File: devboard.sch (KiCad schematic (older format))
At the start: 93 parts, among them J1 Conn_01x04, J2 Conn_02x05_Odd_Even, J3 USB_B_Micro, J4 Conn_01x04, J5 Conn_02x10_Counter_Clockwise, J6 Conn_02x04_Counter_Clockwise, Q1 Q_NPN_BEC, Q2 Q_NPN_BEC, SW1 SW_SPST, U1 ATmega128L-8AU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

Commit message: Remove extraneous wire
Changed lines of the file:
@@
 	1200 1800 1200 1850
 Wire Wire Line
-	1500 1850 1200 1850
-Wire Wire Line
 	1500 2150 1500 2200
 Connection ~ 1500 2200
@@
 Text Label 1900 4900 0    50   ~ 0
 ~OE
-$Comp
-L MCU_Microchip_ATmega:ATmega128L-8AU U1
-U 1 1 5FDDF59E
-P 2650 3900
-F 0 "U1" H 1850 6050 50  0000 C CNN
-F 1 "ATmega128L-8AU" H 2150 5950 50  0000 C CNN
-F 2 "Package_QFP:TQFP-64_14x14mm_P0.8mm" H 2650 3900 50  0001 C CIN
-F 3 "http://ww1.microchip.com/downloads/en/DeviceDoc/doc2467.pdf" H 2650 3900 50  0001 C CNN
-	1    2650 3900
-	1    0    0    -1
-$EndComp
 Wire Wire Line
 	1900 4900 2050 4900
@@
 Wire Wire Line
 	14750 9350 14750 9400
-Connection ~ 14650 1400
-Wire Wire Line
-	14650 1400 15000 1400
 Wire Wire Line
 	8200 4700 8200 4850
@@
 	13600 8600 13600 8650
 Wire Bus Line
-	11700 10350 11700 10750
-Wire Bus Line
-	10700 10350 10700 10750
+	8200 5450 8200 7500
 Wire Bus Line
 	9500 5850 9500 7650
 Wire Bus Line
+	10800 5450 10800 7500
+Wire Bus Line
 	12100 5850 12100 7650
 Wire Bus Line
+	13400 5450 13400 7500
+Wire Bus Line
 	14700 5850 14700 7650
 Wire Bus Line
+	10250 9750 10250 10750
+Wire Bus Line
 	9250 9750 9250 10750
 Wire Bus Line
-	9500 2400 9500 4200
+	11700 10350 11700 10750
 Wire Bus Line
-	12100 2400 12100 4200
+	10700 10350 10700 10750
 Wire Bus Line
-	14700 2400 14700 4200
+	8200 2000 8200 4050
 Wire Bus Line
-	3500 2050 3500 2800
+	9500 2400 9500 4200
 Wire Bus Line
-	10250 9750 10250 10750
+	10800 2000 10800 4050
 Wire Bus Line
-	3500 2950 3500 5500
+	12100 2400 12100 4200
 Wire Bus Line
 	13400 2000 13400 4050
 Wire Bus Line
-	10800 2000 10800 4050
-Wire Bus Line
-	8200 2000 8200 4050
-Wire Bus Line
-	13400 5450 13400 7500
+	14700 2400 14700 4200
 Wire Bus Line
-	10800 5450 10800 7500
+	3500 2950 3500 5500
 Wire Bus Line
-	8200 5450 8200 7500
+	3500 2050 3500 2800
+Wire Wire Line
+	1500 1850 1200 1850
+$Comp
+L MCU_Microchip_ATmega:ATmega128L-8AU U1
+U 1 1 5FDDF59E
+P 2650 3900
+F 0 "U1" H 1850 6050 50  0000 C CNN
+F 1 "ATmega128L-8AU" H 2150 5950 50  0000 C CNN
+F 2 "Package_QFP:TQFP-64_14x14mm_P0.8mm" H 2650 3900 50  0001 C CIN
+F 3 "http://ww1.microchip.com/downloads/en/DeviceDoc/doc2467.pdf" H 2650 3900 50  0001 C CNN
+	1    2650 3900
+	1    0    0    -1
+$EndComp
 $EndSCHEMATC

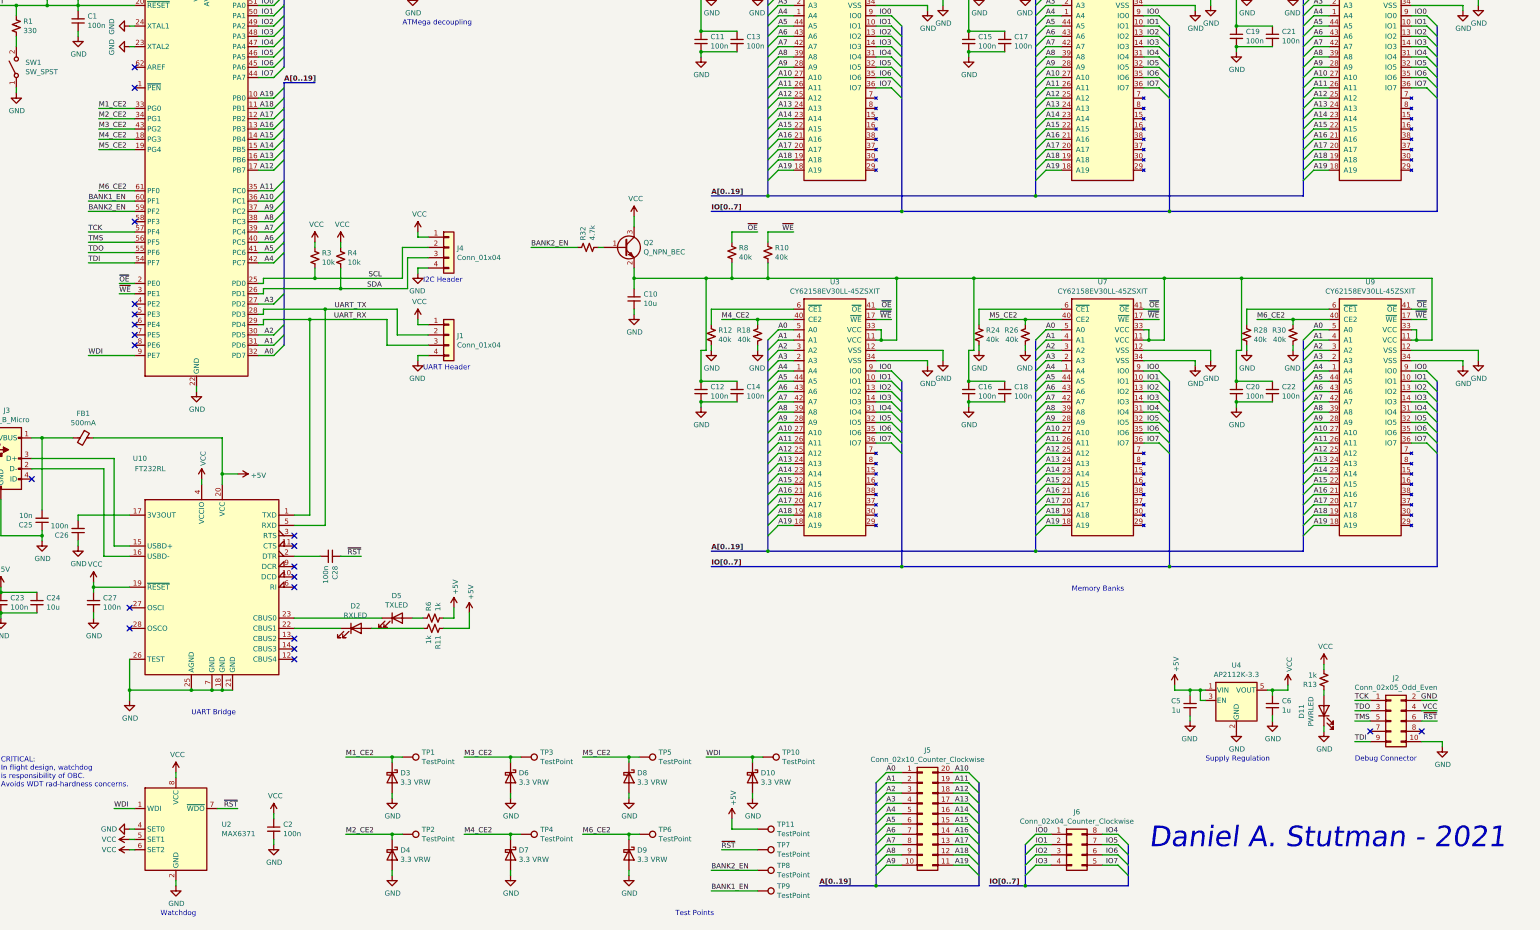
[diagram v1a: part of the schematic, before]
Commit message: SPI programming and silk improvements
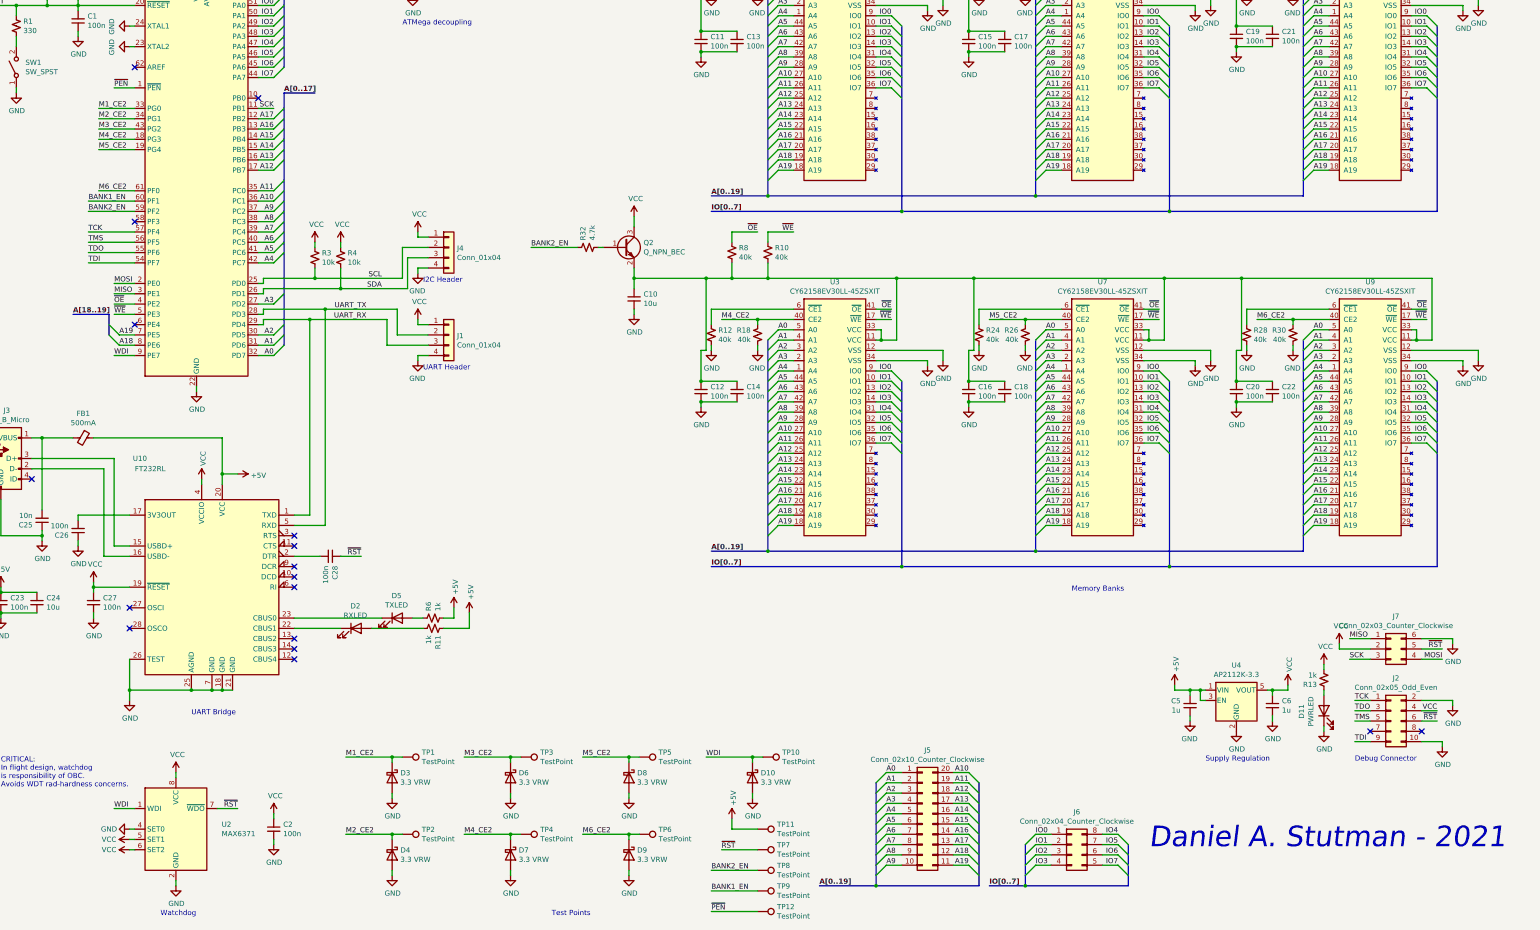
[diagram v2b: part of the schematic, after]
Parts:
- added J7: Conn_02x03_Counter_Clockwise, Connector_PinHeader_1.27mm:PinHeader_2x03_P1.27mm_Vertical, symbol Connector_Generic:Conn_02x03_Counter_Clockwise
- added TP12: TestPoint, Connector_PinHeader_2.54mm:PinHeader_1x01_P2.54mm_Vertical, symbol Connector:TestPoint
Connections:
- net A18: now also U1.8 (PE6); no longer U1.11 (PB1)
- net A19: now also U1.7 (PE5); no longer U1.10 (PB0)
- net GND: now also J7.6 (Pin_6)
- net VCC: now also J7.2 (Pin_2)
- net ~OE: now also U1.4 (PE2); no longer U1.2 (PE0)
- net ~RST: now also J7.5 (Pin_5)
- net ~WE: now also U1.5 (PE3); no longer U1.3 (PE1)
- net ~PEN: now reaches U1.1 (~PEN)
- net ~PEN: now also TP12.1
- new net MISO: J7.1 (Pin_1), U1.3 (PE1)
- new net MOSI: J7.4 (Pin_4), U1.2 (PE0)
- new net SCK: J7.3 (Pin_3), U1.11 (PB1)
- no-connect marks 21 -> 17
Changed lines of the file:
@@
 	1    0    0    -1
 $EndComp
-Text Label 1600 5600 0    50   ~ 0
+Text Label 1850 5600 0    50   ~ 0
 WDI
 Wire Wire Line
-	1600 5600 2050 5600
-Wire Wire Line
 	1600 4400 2050 4400
 Wire Wire Line
@@
 A17
 Entry Wire Line
-	3500 3100 3400 3200
-Text Label 3400 3200 2    50   ~ 0
+	1800 5400 1900 5500
+Text Label 1900 5500 0    50   ~ 0
 A18
 Entry Wire Line
-	3500 3000 3400 3100
-Text Label 3400 3100 2    50   ~ 0
+	1800 5300 1900 5400
+Text Label 1900 5400 0    50   ~ 0
 A19
 Wire Wire Line
@@
 	3400 3300 3250 3300
 Wire Wire Line
-	3400 3200 3250 3200
+	1900 5500 2050 5500
 Wire Wire Line
-	3400 3100 3250 3100
+	1900 5400 2050 5400
 Wire Wire Line
 	3400 3600 3250 3600
@@
 Text Label 3400 4200 2    50   ~ 0
 A9
-Wire Bus Line
-	3500 2950 3800 2950
 Wire Wire Line
 	3300 4850 3300 4900
@@
 Wire Wire Line
 	3300 5300 3250 5300
-Text Label 3500 2950 0    50   ~ 10
-A[0..19]
 Wire Wire Line
 	1700 3200 2050 3200
@@
 TDI
 Wire Wire Line
-	14700 8950 14550 8950
-Wire Wire Line
 	14700 9050 14550 9050
 Wire Wire Line
 	14700 9150 14550 9150
-Text Label 14700 8950 2    50   ~ 0
-GND
 Text Label 14700 9050 2    50   ~ 0
 VCC
@@
 ~RST
 NoConn ~ 14550 9250
-$Comp
-L Connector_Generic:Conn_02x05_Odd_Even J2
-U 1 1 5FDF7679
-P 14250 9150
-F 0 "J2" H 14300 9567 50  0000 C CNN
-F 1 "Conn_02x05_Odd_Even" H 14300 9476 50  0000 C CNN
-F 2 "Connector_PinHeader_1.27mm:PinHeader_2x05_P1.27mm_Vertical" H 14250 9150 50  0001 C CNN
-F 3 "~" H 14250 9150 50  0001 C CNN
-	1    14250 9150
-	1    0    0    -1
-$EndComp
 NoConn ~ 14050 9250
 Text Notes 13900 9550 0    50   ~ 0
@@
 	1    0    0    -1
 $EndComp
-Text Notes 7300 11050 0    50   ~ 0
+Text Notes 6100 11050 0    50   ~ 0
 Test Points
 $Comp
@@
 	3750 5250 4500 5250
 Connection ~ 3750 5250
-NoConn ~ 2050 5100
-NoConn ~ 2050 5200
 NoConn ~ 2050 5300
-NoConn ~ 2050 5400
-NoConn ~ 2050 5500
-NoConn ~ 2050 3000
 NoConn ~ 2050 4300
 Wire Wire Line
@@
 Wire Wire Line
 	8200 4400 8450 4400
-Text Label 1900 5000 0    50   ~ 0
+Text Label 1850 5200 0    50   ~ 0
 ~WE
-Text Label 1900 4900 0    50   ~ 0
+Text Label 1850 5100 0    50   ~ 0
 ~OE
-Wire Wire Line
-	1900 4900 2050 4900
-Wire Wire Line
-	2050 5000 1900 5000
 $Comp
 L power:GND #PWR0121
@@
 Wire Wire Line
 	13600 8600 13600 8650
+Wire Wire Line
+	1500 1850 1200 1850
+$Comp
+L power:GND #PWR0126
+U 1 1 61890DA6
+P 14850 9000
+F 0 "#PWR0126" H 14850 8750 50  0001 C CNN
+F 1 "GND" H 14855 8827 50  0000 C CNN
+F 2 "" H 14850 9000 50  0001 C CNN
+F 3 "" H 14850 9000 50  0001 C CNN
+	1    14850 9000
+	1    0    0    -1
+$EndComp
+$Comp
+L Connector_Generic:Conn_02x05_Odd_Even J2
+U 1 1 5FDF7679
+P 14250 9150
+F 0 "J2" H 14300 9567 50  0000 C CNN
+F 1 "Conn_02x05_Odd_Even" H 14300 9476 50  0000 C CNN
+F 2 "Connector_PinHeader_1.27mm:PinHeader_2x05_P1.27mm_Vertical" H 14250 9150 50  0001 C CNN
+F 3 "~" H 14250 9150 50  0001 C CNN
+	1    14250 9150
+	1    0    0    -1
+$EndComp
+Wire Wire Line
+	14550 8950 14850 8950
+Wire Wire Line
+	14850 8950 14850 9000
+$Comp
+L Connector_Generic:Conn_02x03_Counter_Clockwise J7
+U 1 1 619E5A6C
+P 14250 8450
+F 0 "J7" H 14300 8767 50  0000 C CNN
+F 1 "Conn_02x03_Counter_Clockwise" H 14300 8676 50  0000 C CNN
+F 2 "Connector_PinHeader_1.27mm:PinHeader_2x03_P1.27mm_Vertical" H 14250 8450 50  0001 C CNN
+F 3 "~" H 14250 8450 50  0001 C CNN
+	1    14250 8450
+	1    0    0    -1
+$EndComp
+$Comp
+L power:VCC #PWR0128
+U 1 1 619E68EF
+P 13750 8400
+F 0 "#PWR0128" H 13750 8250 50  0001 C CNN
+F 1 "VCC" H 13765 8573 50  0000 C CNN
+F 2 "" H 13750 8400 50  0001 C CNN
+F 3 "" H 13750 8400 50  0001 C CNN
+	1    13750 8400
+	1    0    0    -1
+$EndComp
+Text Label 1850 4900 0    50   ~ 0
+MOSI
+Text Label 1850 5000 0    50   ~ 0
+MISO
+Text Label 3400 3200 2    50   ~ 0
+SCK
+Wire Wire Line
+	1850 4900 2050 4900
+Wire Wire Line
+	2050 5000 1850 5000
+Wire Wire Line
+	3400 3200 3250 3200
+Text Label 3500 3050 0    50   ~ 10
+A[0..17]
 Wire Bus Line
-	8200 5450 8200 7500
+	3500 3050 3800 3050
+Text Label 1450 5200 0    50   ~ 10
+A[18..19]
 Wire Bus Line
-	9500 5850 9500 7650
+	1450 5200 1800 5200
+$Comp
+L MCU_Microchip_ATmega:ATmega128L-8AU U1
+U 1 1 5FDDF59E
+P 2650 3900
+F 0 "U1" H 1850 6050 50  0000 C CNN
+F 1 "ATmega128L-8AU" H 2150 5950 50  0000 C CNN
+F 2 "Package_QFP:TQFP-64_14x14mm_P0.8mm" H 2650 3900 50  0001 C CIN
+F 3 "http://ww1.microchip.com/downloads/en/DeviceDoc/doc2467.pdf" H 2650 3900 50  0001 C CNN
+	1    2650 3900
+	1    0    0    -1
+$EndComp
+Text Label 1850 3000 0    50   ~ 0
+~PEN
+Wire Wire Line
+	1850 3000 2050 3000
+Text Label 7650 11000 0    50   ~ 0
+~PEN
+$Comp
+L Connector:TestPoint TP12
+U 1 1 62B0EF34
+P 8100 11000
+F 0 "TP12" V 8054 11188 50  0000 L CNN
+F 1 "TestPoint" V 8145 11188 50  0000 L CNN
+F 2 "Connector_PinHeader_2.54mm:PinHeader_1x01_P2.54mm_Vertical" H 8300 11000 50  0001 C CNN
+F 3 "~" H 8300 11000 50  0001 C CNN
+	1    8100 11000
+	0    1    1    0
+$EndComp
+Wire Wire Line
+	7650 11000 8100 11000
+Wire Wire Line
+	1850 5100 2050 5100
+Wire Wire Line
+	1850 5200 2050 5200
+Text Label 14750 8550 2    50   ~ 0
+MOSI
+Text Label 13850 8350 0    50   ~ 0
+MISO
+Wire Wire Line
+	14750 8550 14550 8550
+Wire Wire Line
+	14050 8350 13850 8350
+Text Label 13850 8550 0    50   ~ 0
+SCK
+NoConn ~ 3250 3100
+Wire Wire Line
+	13750 8450 13750 8400
+Wire Wire Line
+	13750 8450 14050 8450
+$Comp
+L power:GND #PWR0130
+U 1 1 61B3CB80
+P 14850 8400
+F 0 "#PWR0130" H 14850 8150 50  0001 C CNN
+F 1 "GND" H 14855 8227 50  0000 C CNN
+F 2 "" H 14850 8400 50  0001 C CNN
+F 3 "" H 14850 8400 50  0001 C CNN
+	1    14850 8400
+	1    0    0    -1
+$EndComp
+Wire Wire Line
+	14850 8400 14850 8350
+Wire Wire Line
+	14850 8350 14550 8350
+Text Label 14750 8450 2    50   ~ 0
+~RST
+Wire Wire Line
+	14550 8450 14750 8450
+Wire Wire Line
+	1850 5600 2050 5600
+Wire Wire Line
+	13850 8550 14050 8550
 Wire Bus Line
-	10800 5450 10800 7500
+	1800 5200 1800 5400
 Wire Bus Line
-	12100 5850 12100 7650
+	11700 10350 11700 10750
 Wire Bus Line
-	13400 5450 13400 7500
+	10700 10350 10700 10750
 Wire Bus Line
-	14700 5850 14700 7650
+	9500 5850 9500 7650
 Wire Bus Line
-	10250 9750 10250 10750
+	12100 5850 12100 7650
+Wire Bus Line
+	14700 5850 14700 7650
 Wire Bus Line
 	9250 9750 9250 10750
 Wire Bus Line
-	11700 10350 11700 10750
+	9500 2400 9500 4200
 Wire Bus Line
-	10700 10350 10700 10750
+	12100 2400 12100 4200
 Wire Bus Line
-	8200 2000 8200 4050
+	14700 2400 14700 4200
 Wire Bus Line
-	9500 2400 9500 4200
+	3500 2050 3500 2800
 Wire Bus Line
-	10800 2000 10800 4050
+	10250 9750 10250 10750
 Wire Bus Line
-	12100 2400 12100 4200
+	3500 3050 3500 5500
 Wire Bus Line
 	13400 2000 13400 4050
 Wire Bus Line
-	14700 2400 14700 4200
+	10800 2000 10800 4050
 Wire Bus Line
-	3500 2950 3500 5500
+	8200 2000 8200 4050
 Wire Bus Line
-	3500 2050 3500 2800
-Wire Wire Line
-	1500 1850 1200 1850
-$Comp
-L MCU_Microchip_ATmega:ATmega128L-8AU U1
-U 1 1 5FDDF59E
-P 2650 3900
-F 0 "U1" H 1850 6050 50  0000 C CNN
-F 1 "ATmega128L-8AU" H 2150 5950 50  0000 C CNN
-F 2 "Package_QFP:TQFP-64_14x14mm_P0.8mm" H 2650 3900 50  0001 C CIN
-F 3 "http://ww1.microchip.com/downloads/en/DeviceDoc/doc2467.pdf" H 2650 3900 50  0001 C CNN
-	1    2650 3900
-	1    0    0    -1
-$EndComp
+	13400 5450 13400 7500
+Wire Bus Line
+	10800 5450 10800 7500
+Wire Bus Line
+	8200 5450 8200 7500
 $EndSCHEMATC
